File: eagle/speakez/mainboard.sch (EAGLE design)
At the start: 28 parts, among them U1 +12v

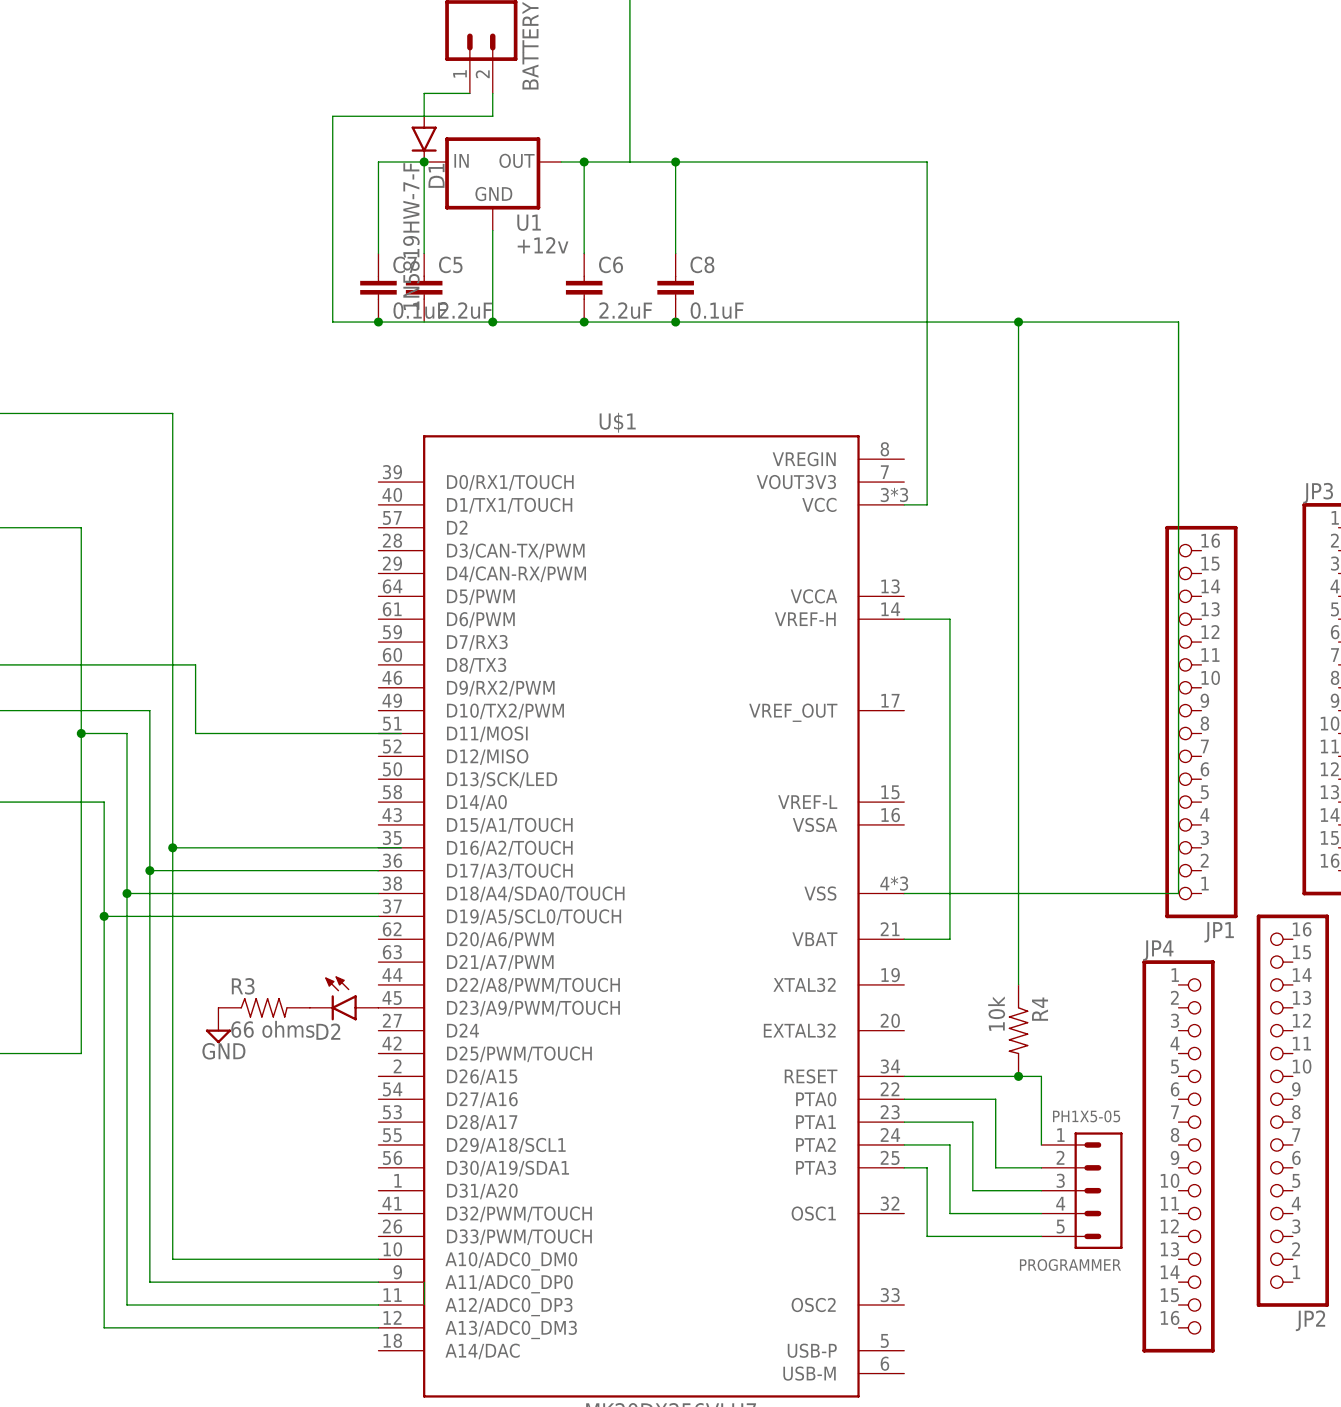
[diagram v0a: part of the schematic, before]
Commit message: added serial header connected to TX/RX
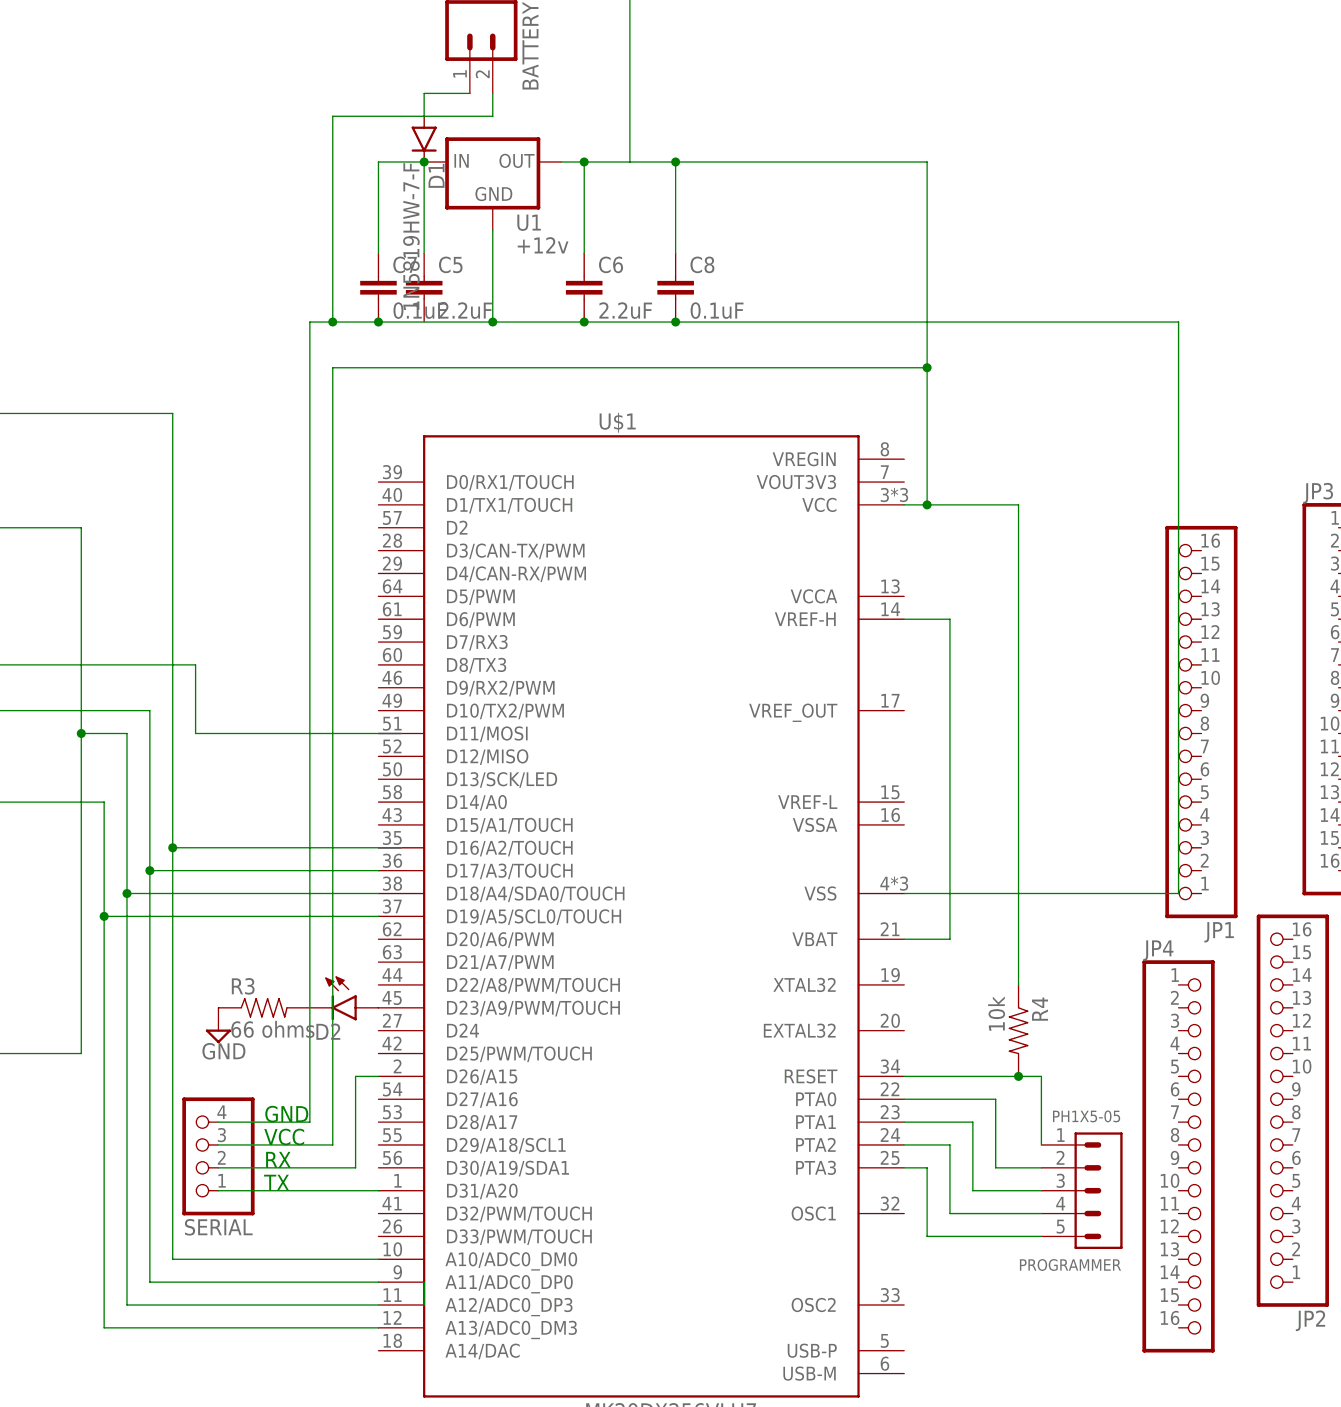
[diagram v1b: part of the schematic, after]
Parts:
- added SERIAL: (no value), pinhead:PINHD-1X4
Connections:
- new net N$25: SERIAL.1, U$1.D31/A20
- new net N$26: SERIAL.2, U$1.D26/A15
- net N$14: now also SERIAL.4; no longer R4.1
- net N$16: now also R4.1, SERIAL.3
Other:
- note added: "RX"
- note added: "TX"
- note added: "VCC"
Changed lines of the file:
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@@
 <part name="R4" library="SparkFun-Passives" deviceset="RESISTOR" device="0805-RES" value="10k"/>
 <part name="PROGRAMMER" library="pel_hdr" deviceset="PH1X5" device="-05"/>
+<part name="SERIAL" library="pinhead" deviceset="PINHD-1X4" device=""/>
 </parts>
 <sheets>
@@
 <text x="33.02" y="63.5" size="1.778" layer="91" rot="R90">GND</text>
 <text x="30.48" y="63.5" size="1.778" layer="91" rot="R90">CLK</text>
+<text x="104.14" y="-5.08" size="1.778" layer="91">GND</text>
+<text x="104.14" y="-7.62" size="1.778" layer="91">VCC</text>
+<text x="104.14" y="-12.7" size="1.778" layer="91">TX</text>
+<text x="104.14" y="-10.16" size="1.778" layer="91">RX</text>
 </plain>
 <instances>
@@
 <instance part="R4" gate="G$1" x="187.96" y="5.08" rot="R270"/>
 <instance part="PROGRAMMER" gate="G$1" x="198.12" y="-7.62" rot="R180"/>
+<instance part="SERIAL" gate="A" x="96.52" y="-7.62" rot="R180"/>
 </instances>
 <busses>
@@
 <wire x1="139.7" y1="83.82" x2="149.86" y2="83.82" width="0.1524" layer="91"/>
 <junction x="139.7" y="83.82"/>
-<wire x1="149.86" y1="83.82" x2="187.96" y2="83.82" width="0.1524" layer="91"/>
-<wire x1="187.96" y1="83.82" x2="205.74" y2="83.82" width="0.1524" layer="91"/>
+<wire x1="149.86" y1="83.82" x2="205.74" y2="83.82" width="0.1524" layer="91"/>
 <wire x1="205.74" y1="83.82" x2="205.74" y2="20.32" width="0.1524" layer="91"/>
 <pinref part="U$1" gate="G$1" pin="VSS"/>
@@
 <pinref part="C8" gate="G$1" pin="2"/>
 <junction x="149.86" y="83.82"/>
-<pinref part="R4" gate="G$1" pin="1"/>
-<wire x1="187.96" y1="10.16" x2="187.96" y2="83.82" width="0.1524" layer="91"/>
-<junction x="187.96" y="83.82"/>
+<wire x1="111.76" y1="83.82" x2="109.22" y2="83.82" width="0.1524" layer="91"/>
+<junction x="111.76" y="83.82"/>
+<wire x1="109.22" y1="83.82" x2="109.22" y2="-5.08" width="0.1524" layer="91"/>
+<pinref part="SERIAL" gate="A" pin="4"/>
+<wire x1="109.22" y1="-5.08" x2="99.06" y2="-5.08" width="0.1524" layer="91"/>
 </segment>
 </net>
@@
 <wire x1="144.78" y1="101.6" x2="149.86" y2="101.6" width="0.1524" layer="91"/>
 <wire x1="149.86" y1="101.6" x2="177.8" y2="101.6" width="0.1524" layer="91"/>
-<wire x1="177.8" y1="101.6" x2="177.8" y2="63.5" width="0.1524" layer="91"/>
+<wire x1="177.8" y1="101.6" x2="177.8" y2="78.74" width="0.1524" layer="91"/>
 <pinref part="U$1" gate="G$1" pin="VCC"/>
+<wire x1="177.8" y1="78.74" x2="177.8" y2="63.5" width="0.1524" layer="91"/>
 <wire x1="177.8" y1="63.5" x2="175.26" y2="63.5" width="0.1524" layer="91"/>
 <pinref part="C8" gate="G$1" pin="1"/>
 <wire x1="149.86" y1="91.44" x2="149.86" y2="101.6" width="0.1524" layer="91"/>
 <junction x="149.86" y="101.6"/>
+<wire x1="177.8" y1="63.5" x2="187.96" y2="63.5" width="0.1524" layer="91"/>
+<junction x="177.8" y="63.5"/>
+<pinref part="R4" gate="G$1" pin="1"/>
+<wire x1="187.96" y1="63.5" x2="187.96" y2="10.16" width="0.1524" layer="91"/>
+<wire x1="177.8" y1="78.74" x2="111.76" y2="78.74" width="0.1524" layer="91"/>
+<junction x="177.8" y="78.74"/>
+<wire x1="111.76" y1="78.74" x2="111.76" y2="-7.62" width="0.1524" layer="91"/>
+<pinref part="SERIAL" gate="A" pin="3"/>
+<wire x1="111.76" y1="-7.62" x2="99.06" y2="-7.62" width="0.1524" layer="91"/>
 </segment>
 </net>
@@
 </segment>
 </net>
+<net name="N$25" class="0">
+<segment>
+<pinref part="SERIAL" gate="A" pin="1"/>
+<pinref part="U$1" gate="G$1" pin="D31/A20"/>
+<wire x1="99.06" y1="-12.7" x2="116.84" y2="-12.7" width="0.1524" layer="91"/>
+</segment>
+</net>
+<net name="N$26" class="0">
+<segment>
+<pinref part="U$1" gate="G$1" pin="D26/A15"/>
+<wire x1="116.84" y1="0" x2="114.3" y2="0" width="0.1524" layer="91"/>
+<wire x1="114.3" y1="0" x2="114.3" y2="-10.16" width="0.1524" layer="91"/>
+<pinref part="SERIAL" gate="A" pin="2"/>
+<wire x1="114.3" y1="-10.16" x2="99.06" y2="-10.16" width="0.1524" layer="91"/>
+</segment>
+</net>
